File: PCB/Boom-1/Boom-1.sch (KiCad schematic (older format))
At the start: 705 parts, among them J1 NoiseIOConn, J10 Osc1HFTrackConn, J11 Osc1FiltCVConn, J12 OscFiltEnv1Conn, J13 OscFiltEnv2Conn, J14 SubFiltEnv1Conn, J15 SubFiltEnv2Conn, J16 Osc1FXConn, J17 SubFXConn, J18 Osc1FiltCVConn, J19 Osc1FiltCVConn, J2 Conn_01x07, J20 Osc2FXConn, J21 OscAmpEnvConn, J22 SubAmpEnvConn, J23 OscAmpEnvBypass, J24 SubAmpAudioBypass, J25 SubAmpEnvBypass, J26 PreFV1FXConn, J27 PowerConn, J28 FV1Conn, J29 IOConn, J3 Osc1CVConn, J4 Osc2SyncConn, J5 Osc1SyncConn, J6 Osc2ScaleConn, J7 Osc2HFTrackConn, J8 Conn_01x03, J9 Osc1ScaleConn, Q1 2N3904, SW1 SW_DIP_x04, U1 CEM3340, U10 AS3320, U11 AS3310, U12 AS3310, U13 AS3310, U14 AS3310, U15 V2164D, U16 AS3310, U17 AS3310, U18 V2164D, U19 TL074, U2 CEM3340, U20 TL074, U21 TL072, U22 TL074, U23 TL074, U24 TL074, U25 TL074, U26 TL074, U27 TL072, U28 TL074, U29 TL072, U3 4013, U30 TL074, U31 TL072, U32 TL074, U33 TL074, U34 TL074, U35 TL072, U36 TL074, U37 TL074, U38 TL072, U39 TL074, U4 NOISE, U40 TL072, U41 TL074, U42 TL074, U43 TL074, U44 TL074, U45 L7905, U46 L7805, U47 TL072, U48 TL072, U5 V2164D, U6 V2164D, U7 V2164D, U8 AS3320, U9 AS3320

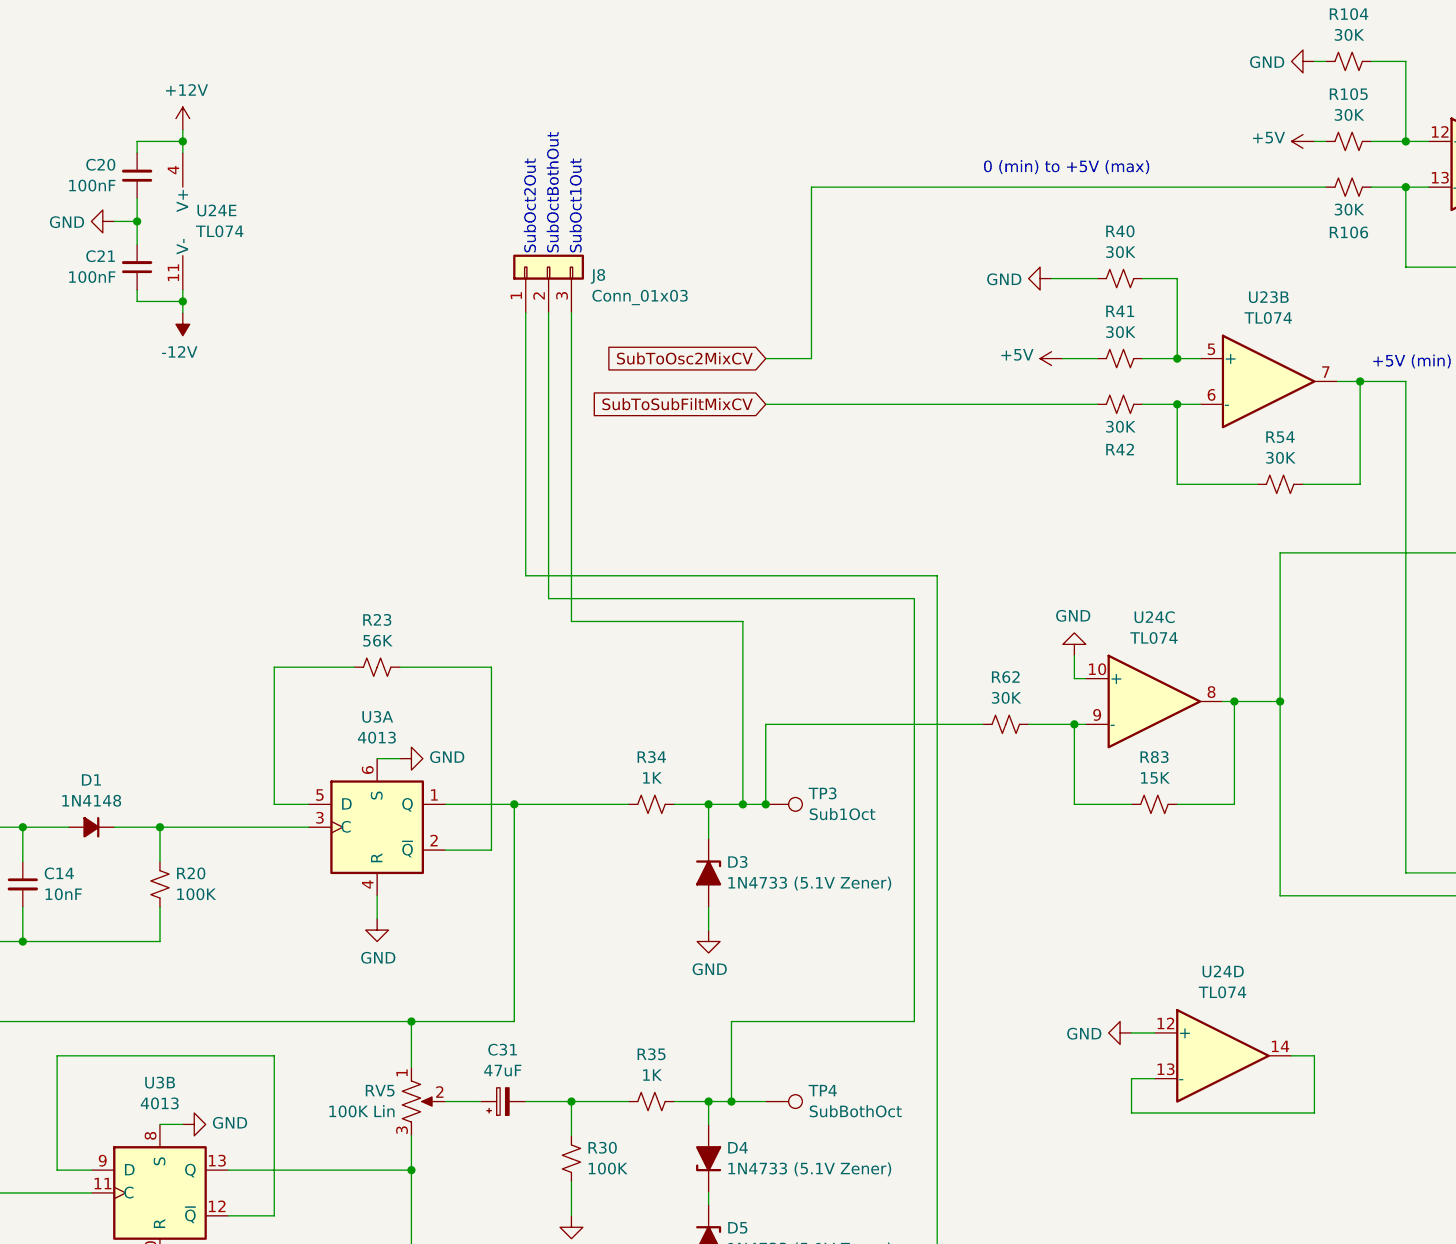
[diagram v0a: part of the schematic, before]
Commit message: swapped u24 to a tl072
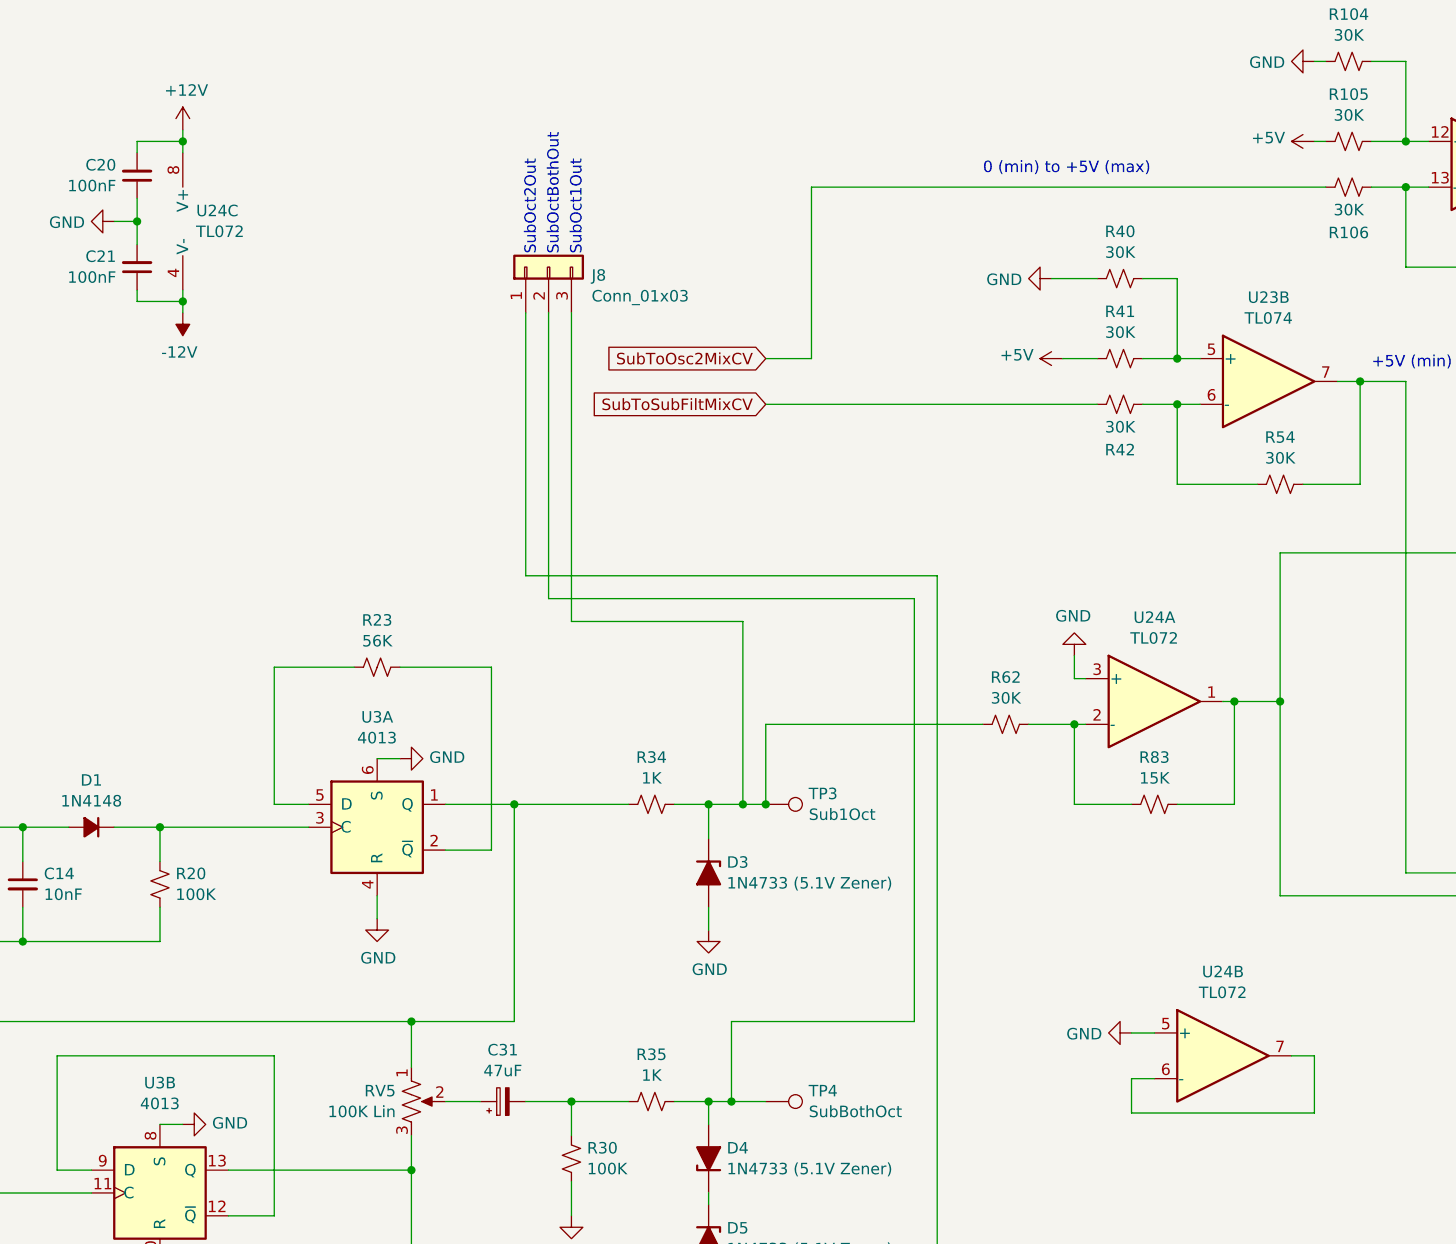
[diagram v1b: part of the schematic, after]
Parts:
- removed U24: TL074, Package_DIP:DIP-14_W7.62mm, symbol Amplifier_Operational:TL074
- added U24: TL072, Package_DIP:DIP-8_W7.62mm, symbol Amplifier_Operational:TL072
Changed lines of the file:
@@
 $EndComp
 $Comp
-L Amplifier_Operational:TL074 U24
-U 3 1 690BEF49
-P 12650 40400
-F 0 "U24" H 12650 40767 50  0000 C CNN
-F 1 "TL074" H 12650 40676 50  0000 C CNN
-F 2 "Package_DIP:DIP-14_W7.62mm" H 12600 40500 50  0001 C CNN
-F 3 "http://www.ti.com/lit/ds/symlink/tl071.pdf" H 12700 40600 50  0001 C CNN
-	3    12650 40400
-	1    0    0    -1
-$EndComp
-$Comp
 L 4xxx:4013 U3
 U 3 1 690C6830
@@
 	8750 25800 8750 25850
 $Comp
-L Amplifier_Operational:TL074 U24
-U 5 1 6E429D4A
-P 8500 38300
-F 0 "U24" H 8458 38346 50  0000 L CNN
-F 1 "TL074" H 8458 38255 50  0000 L CNN
-F 2 "Package_DIP:DIP-14_W7.62mm" H 8450 38400 50  0001 C CNN
-F 3 "http://www.ti.com/lit/ds/symlink/tl071.pdf" H 8550 38500 50  0001 C CNN
-	5    8500 38300
-	1    0    0    -1
-$EndComp
-$Comp
 L power:+12V #PWR037
 U 1 1 6E429DAC
@@
 	15400 33000 15300 33000
 $Comp
-L Amplifier_Operational:TL074 U24
-U 4 1 62C50A04
-P 12950 41950
-F 0 "U24" H 12950 42317 50  0000 C CNN
-F 1 "TL074" H 12950 42226 50  0000 C CNN
-F 2 "Package_DIP:DIP-14_W7.62mm" H 12900 42050 50  0001 C CNN
-F 3 "http://www.ti.com/lit/ds/symlink/tl071.pdf" H 13000 42150 50  0001 C CNN
-	4    12950 41950
-	1    0    0    -1
-$EndComp
-$Comp
 L power:GND #PWR0365
 U 1 1 62C50A66
@@
 Wire Wire Line
 	10100 40050 10850 40050
+$Comp
+L Amplifier_Operational:TL072 U24
+U 3 1 626B162E
+P 8500 38300
+F 0 "U24" H 8458 38346 50  0000 L CNN
+F 1 "TL072" H 8458 38255 50  0000 L CNN
+F 2 "Package_DIP:DIP-8_W7.62mm" H 8500 38300 50  0001 C CNN
+F 3 "http://www.ti.com/lit/ds/symlink/tl071.pdf" H 8500 38300 50  0001 C CNN
+	3    8500 38300
+	1    0    0    -1
+$EndComp
+$Comp
+L Amplifier_Operational:TL072 U24
+U 1 1 626BB8DD
+P 12650 40400
+F 0 "U24" H 12650 40767 50  0000 C CNN
+F 1 "TL072" H 12650 40676 50  0000 C CNN
+F 2 "Package_DIP:DIP-8_W7.62mm" H 12650 40400 50  0001 C CNN
+F 3 "http://www.ti.com/lit/ds/symlink/tl071.pdf" H 12650 40400 50  0001 C CNN
+	1    12650 40400
+	1    0    0    -1
+$EndComp
+$Comp
+L Amplifier_Operational:TL072 U24
+U 2 1 626C59CD
+P 12950 41950
+F 0 "U24" H 12950 42317 50  0000 C CNN
+F 1 "TL072" H 12950 42226 50  0000 C CNN
+F 2 "Package_DIP:DIP-8_W7.62mm" H 12950 41950 50  0001 C CNN
+F 3 "http://www.ti.com/lit/ds/symlink/tl071.pdf" H 12950 41950 50  0001 C CNN
+	2    12950 41950
+	1    0    0    -1
+$EndComp
 $EndSCHEMATC

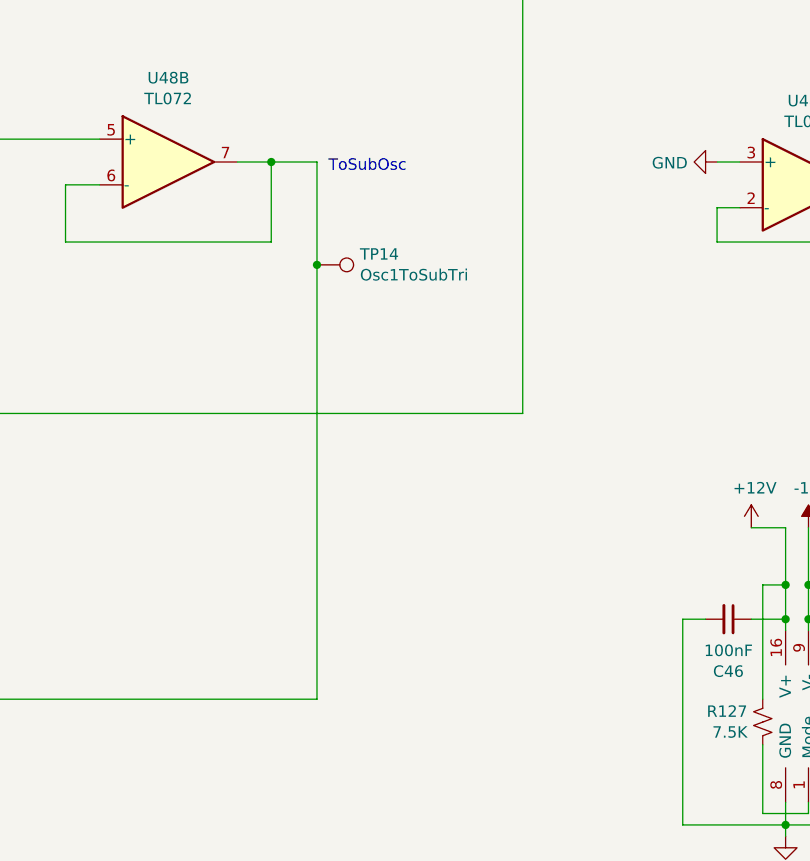
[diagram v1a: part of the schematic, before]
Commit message: moved sub osc into place
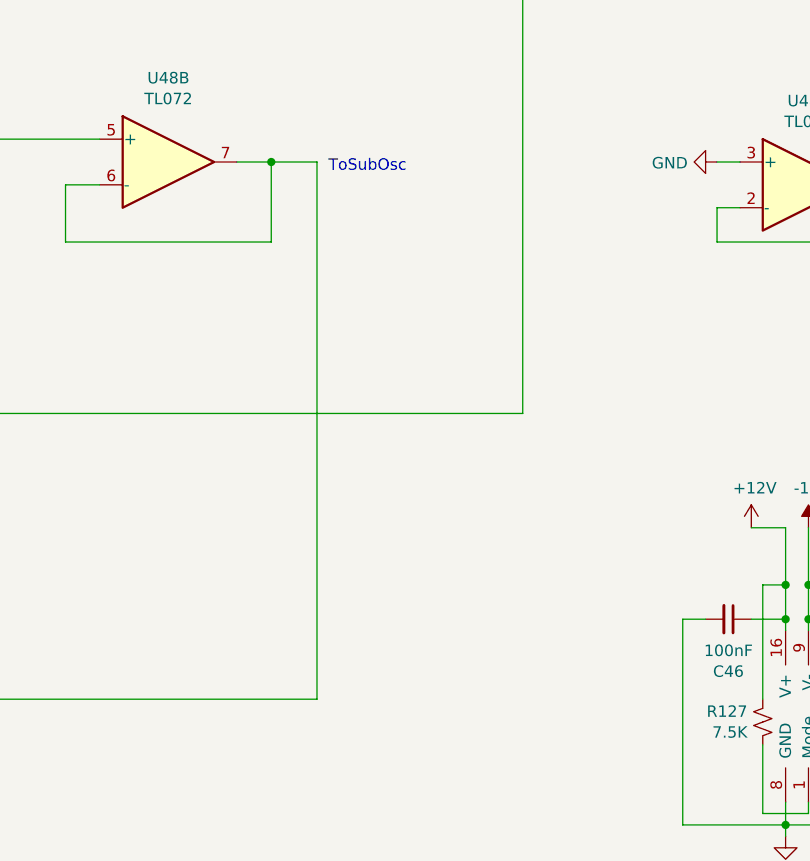
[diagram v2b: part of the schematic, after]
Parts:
- removed TP14: Osc1ToSubTri, Connector_PinHeader_2.54mm:PinHeader_1x01_P2.54mm_Vertical, symbol Connector:TestPoint
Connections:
- wire segments 3050 -> 3049
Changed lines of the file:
@@
 Wire Wire Line
 	12650 32900 12850 32900
-Wire Wire Line
-	12850 32900 12850 33350
 Connection ~ 12650 32900
 Text Notes 12900 32950 0    50   ~ 0
@@
 Wire Wire Line
 	13750 31950 13750 31550
-$Comp
-L Connector:TestPoint TP14
-U 1 1 6FA02700
-P 12850 33350
-F 0 "TP14" V 12804 33538 50  0000 L CNN
-F 1 "Osc1ToSubTri" V 12895 33538 50  0000 L CNN
-F 2 "Connector_PinHeader_2.54mm:PinHeader_1x01_P2.54mm_Vertical" H 13050 33350 50  0001 C CNN
-F 3 "~" H 13050 33350 50  0001 C CNN
-	1    12850 33350
-	0    1    1    0
-$EndComp
-Connection ~ 12850 33350
-Wire Wire Line
-	12850 33350 12850 35250
 Wire Wire Line
 	10850 31750 10950 31750
@@
 	1    0    0    -1
 $EndComp
+Wire Wire Line
+	12850 32900 12850 35250
 $EndSCHEMATC
